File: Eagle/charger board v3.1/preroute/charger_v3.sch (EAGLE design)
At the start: 32 parts, among them IC1 IR2110D, Q1 2N7000, Q2 IRFP240, Q3 MJE13003G

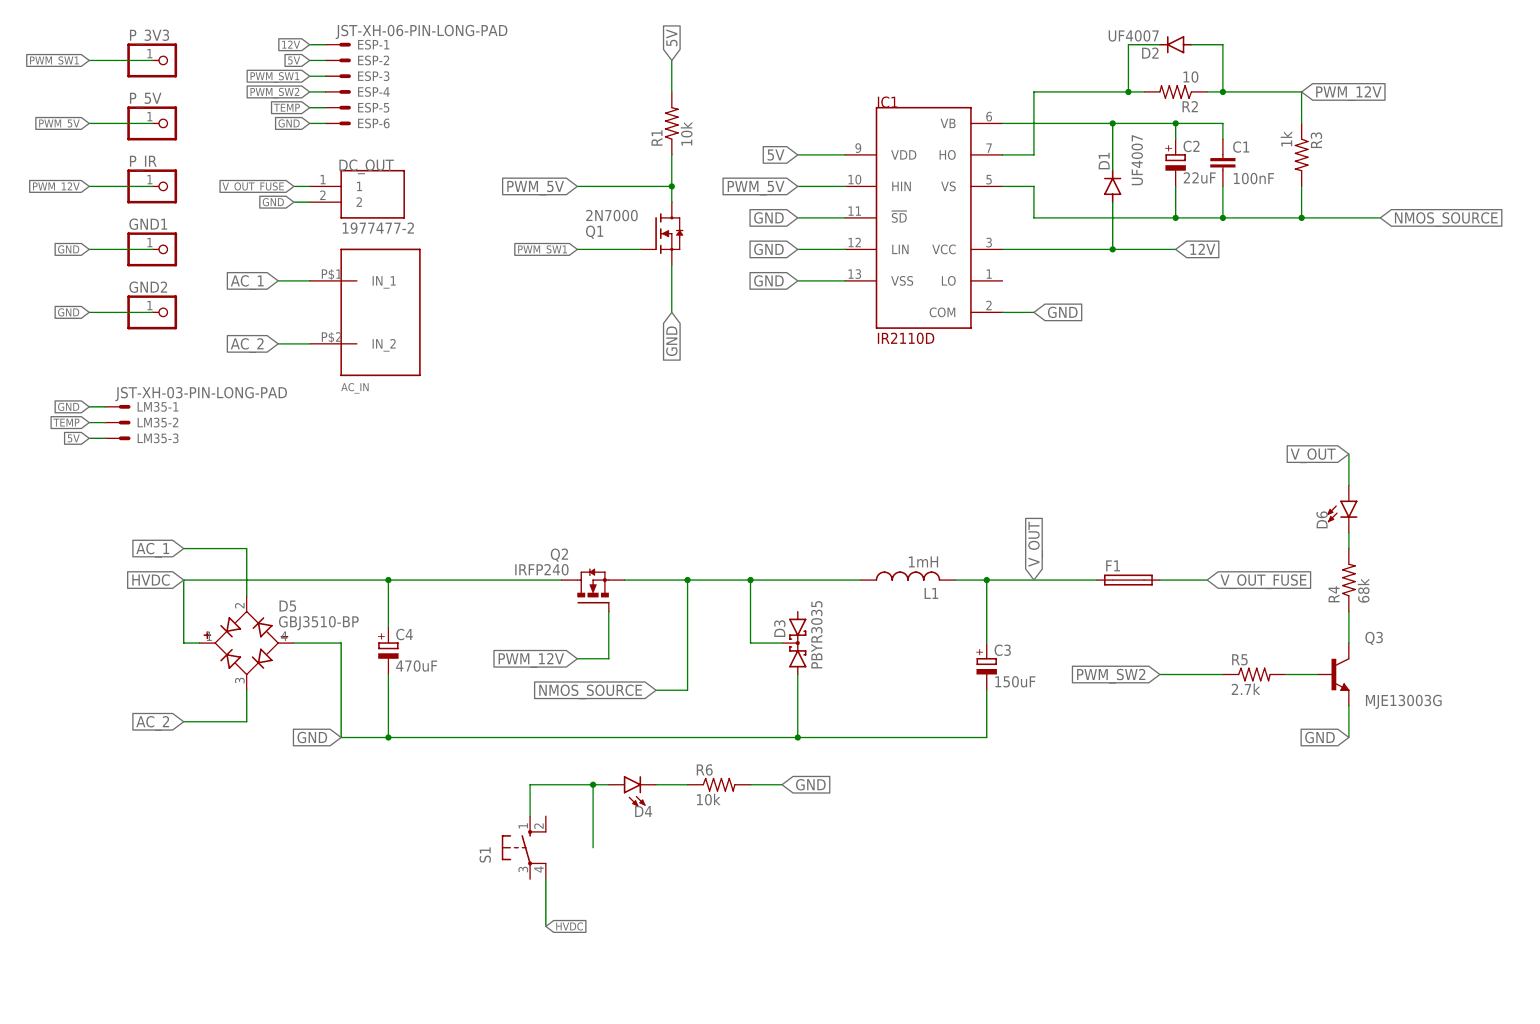
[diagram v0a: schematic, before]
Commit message: buat board charger v3.1
spdt relay
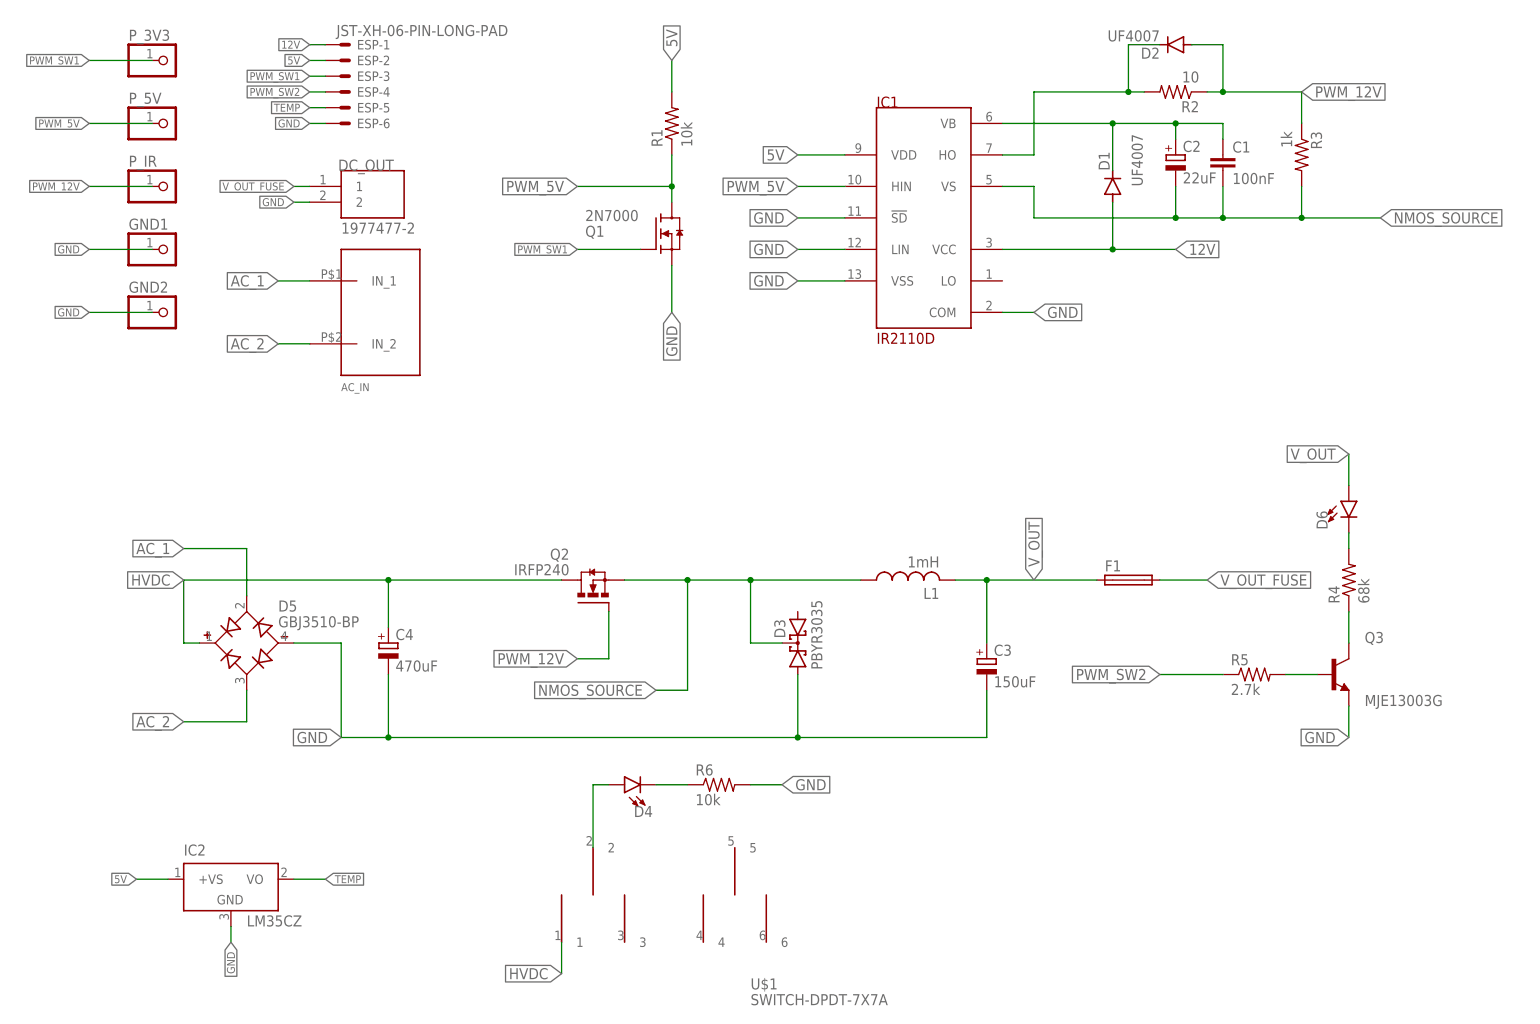
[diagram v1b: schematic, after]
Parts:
- removed LM35: JST-XH-03-PIN-LONG-PAD, Rembrandt Electronics - JST XH Connectors v1-0:JST-XH-03-PIN-LONG-PAD
- removed S1: (no value), switch-omron:10-XX
- added IC2: LM35CZ, lm35:LM35CZ
- added U$1: SWITCH-DPDT-7X7A, TA_library:SWITCH-DPDT-7X7A
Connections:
- net 5V: now also IC2.+VS; no longer LM35-3.S
- net GND: now also IC2.GND; no longer LM35-1.S
- net HVDC: now also U$1.1; no longer S1.P1
- net N$2: now also U$1.2; no longer S1.S
- net TEMP: now also IC2.VO; no longer LM35-2.S
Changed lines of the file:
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@@
 <part name="R5" library="rcl" library_urn="urn:adsk.eagle:library:334" deviceset="R-US_" device="0204/7" package3d_urn="urn:adsk.eagle:package:23498/2" value="2.7k"/>
 <part name="ESP" library="Rembrandt Electronics - JST XH Connectors v1-0" deviceset="JST-XH-06-PIN" device="-LONG-PAD"/>
+<part name="IC2" library="lm35" deviceset="LM35" device="CZ"/>
 <part name="P_3V3" library="pinhead" library_urn="urn:adsk.eagle:library:325" deviceset="PINHD-1X1" device="" package3d_urn="urn:adsk.eagle:package:22485/2"/>
 <part name="P_5V" library="pinhead" library_urn="urn:adsk.eagle:library:325" deviceset="PINHD-1X1" device="" package3d_urn="urn:adsk.eagle:package:22485/2"/>
@@
 <part name="FRAME1" library="frames" library_urn="urn:adsk.eagle:library:229" deviceset="A4L-LOC" device=""/>
 <part name="F1" library="fuse" library_urn="urn:adsk.eagle:library:233" deviceset="SH25" device="" package3d_urn="urn:adsk.eagle:package:14066/1"/>
+<part name="U$1" library="TA_library" deviceset="SWITCH-DPDT-7X7" device="A"/>
 <part name="R6" library="rcl" library_urn="urn:adsk.eagle:library:334" deviceset="R-US_" device="0204/7" package3d_urn="urn:adsk.eagle:package:23498/2" value="10k"/>
 <part name="D4" library="Sparkfun_LED" deviceset="LED" device="5MM"/>
@@
 <part name="AC_IN" library="TA_library" deviceset="XT90" device="A"/>
 <part name="GND2" library="pinhead" library_urn="urn:adsk.eagle:library:325" deviceset="PINHD-1X1" device="" package3d_urn="urn:adsk.eagle:package:22485/2"/>
-<part name="S1" library="switch-omron" library_urn="urn:adsk.eagle:library:377" deviceset="10-XX" device="" package3d_urn="urn:adsk.eagle:package:27496/1"/>
-<part name="LM35" library="Rembrandt Electronics - JST XH Connectors v1-0" deviceset="JST-XH-03-PIN" device="-LONG-PAD"/>
 </parts>
 <sheets>
@@
 <attribute name="NAME" x="12.7" y="50.038" size="1.524" layer="95"/>
 </instance>
+<instance part="IC2" gate="G$1" x="-7.62" y="-71.12" smashed="yes">
+<attribute name="NAME" x="-15.24" y="-67.31" size="1.778" layer="95"/>
+<attribute name="VALUE" x="-5.08" y="-78.74" size="1.778" layer="96"/>
+</instance>
 <instance part="P_3V3" gate="G$1" x="-17.78" y="60.96" smashed="yes">
 <attribute name="NAME" x="-24.13" y="64.135" size="1.778" layer="95"/>
@@
 <attribute name="VALUE" x="133.35" y="-25.781" size="1.778" layer="96"/>
 </instance>
+<instance part="U$1" gate="G$1" x="83.82" y="-78.74" smashed="yes">
+<attribute name="NAME" x="76.2" y="-88.9" size="1.778" layer="95"/>
+<attribute name="VALUE" x="76.2" y="-91.44" size="1.778" layer="96"/>
+</instance>
 <instance part="R6" gate="G$1" x="71.12" y="-55.88" smashed="yes">
 <attribute name="NAME" x="67.31" y="-54.3814" size="1.778" layer="95"/>
@@
 <attribute name="NAME" x="-24.13" y="23.495" size="1.778" layer="95"/>
 <attribute name="VALUE" x="-24.13" y="15.24" size="1.778" layer="96"/>
-</instance>
-<instance part="S1" gate="1" x="40.64" y="-66.04" smashed="yes">
-<attribute name="NAME" x="34.29" y="-68.58" size="1.778" layer="95" rot="R90"/>
-<attribute name="VALUE" x="36.83" y="-62.865" size="1.778" layer="96" rot="R90"/>
-</instance>
-<instance part="LM35" gate="-1" x="-25.4" y="5.08" smashed="yes">
-<attribute name="NAME" x="-22.86" y="4.318" size="1.524" layer="95"/>
-<attribute name="VALUE" x="-26.162" y="6.477" size="1.778" layer="96"/>
-</instance>
-<instance part="LM35" gate="-2" x="-25.4" y="2.54" smashed="yes">
-<attribute name="NAME" x="-22.86" y="1.778" size="1.524" layer="95"/>
-</instance>
-<instance part="LM35" gate="-3" x="-25.4" y="0" smashed="yes">
-<attribute name="NAME" x="-22.86" y="-0.762" size="1.524" layer="95"/>
 </instance>
 </instances>
@@
 </segment>
 <segment>
+<pinref part="IC2" gate="G$1" pin="GND"/>
+<wire x1="-7.62" y1="-78.74" x2="-7.62" y2="-81.28" width="0.1524" layer="91"/>
+<label x="-7.62" y="-81.28" size="1.27" layer="95" rot="R270" xref="yes"/>
+</segment>
+<segment>
 <pinref part="GND1" gate="G$1" pin="1"/>
 <wire x1="-20.32" y1="30.48" x2="-30.48" y2="30.48" width="0.1524" layer="91"/>
@@
 <label x="-30.48" y="20.32" size="1.27" layer="95" rot="R180" xref="yes"/>
 </segment>
-<segment>
-<pinref part="LM35" gate="-1" pin="S"/>
-<wire x1="-27.94" y1="5.08" x2="-30.48" y2="5.08" width="0.1524" layer="91"/>
-<label x="-30.48" y="5.08" size="1.27" layer="95" rot="R180" xref="yes"/>
-</segment>
 </net>
 <net name="5V" class="0">
@@
 </segment>
 <segment>
-<pinref part="LM35" gate="-3" pin="S"/>
-<wire x1="-27.94" y1="0" x2="-30.48" y2="0" width="0.1524" layer="91"/>
-<label x="-30.48" y="0" size="1.27" layer="95" rot="R180" xref="yes"/>
+<pinref part="IC2" gate="G$1" pin="+VS"/>
+<wire x1="-17.78" y1="-71.12" x2="-22.86" y2="-71.12" width="0.1524" layer="91"/>
+<label x="-22.86" y="-71.12" size="1.27" layer="95" rot="R180" xref="yes"/>
 </segment>
 </net>
@@
 </segment>
 <segment>
-<pinref part="S1" gate="1" pin="P1"/>
-<wire x1="43.18" y1="-71.12" x2="43.18" y2="-78.74" width="0.1524" layer="91"/>
-<label x="43.18" y="-78.74" size="1.27" layer="95" xref="yes"/>
+<pinref part="U$1" gate="G$1" pin="1"/>
+<wire x1="45.72" y1="-81.28" x2="45.72" y2="-86.36" width="0.1524" layer="91"/>
+<label x="45.72" y="-86.36" size="1.778" layer="95" rot="R180" xref="yes"/>
 </segment>
 </net>
@@
 </segment>
 <segment>
-<pinref part="LM35" gate="-2" pin="S"/>
-<wire x1="-27.94" y1="2.54" x2="-30.48" y2="2.54" width="0.1524" layer="91"/>
-<label x="-30.48" y="2.54" size="1.27" layer="95" rot="R180" xref="yes"/>
+<pinref part="IC2" gate="G$1" pin="VO"/>
+<wire x1="2.54" y1="-71.12" x2="7.62" y2="-71.12" width="0.1524" layer="91"/>
+<label x="7.62" y="-71.12" size="1.27" layer="95" xref="yes"/>
 </segment>
 </net>
@@
 <pinref part="D4" gate="D1" pin="A"/>
 <wire x1="53.34" y1="-55.88" x2="50.8" y2="-55.88" width="0.1524" layer="91"/>
+<pinref part="U$1" gate="G$1" pin="2"/>
 <wire x1="50.8" y1="-55.88" x2="50.8" y2="-66.04" width="0.1524" layer="91"/>
-<pinref part="S1" gate="1" pin="S"/>
-<wire x1="40.64" y1="-60.96" x2="40.64" y2="-55.88" width="0.1524" layer="91"/>
-<wire x1="40.64" y1="-55.88" x2="50.8" y2="-55.88" width="0.1524" layer="91"/>
-<junction x="50.8" y="-55.88"/>
-</segment>
-</net>
+</segment>
+</net>
